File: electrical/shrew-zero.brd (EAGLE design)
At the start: 18 x 20 mm, 44 parts, among them IC1 LMR16006YQ3DDCTQ1, U1 ESP32-PICO-D4, U2 SX1280IMLTRT, X1 PIN-1X-BIG, X2 PIN-1X-BIG, Y1 2450FM07D0034001T, Y2 52MHz TCXO

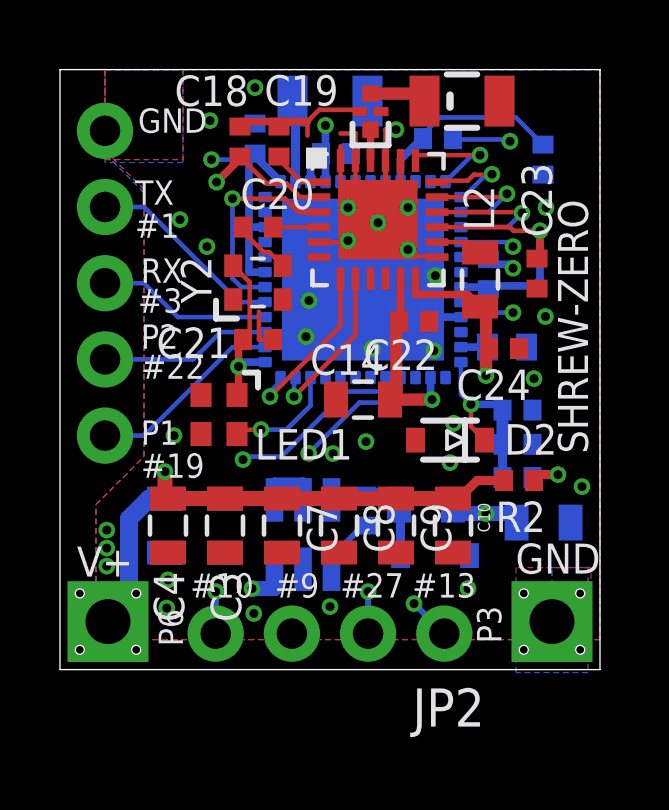
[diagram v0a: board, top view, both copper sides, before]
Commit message: shrew zero layout improvements
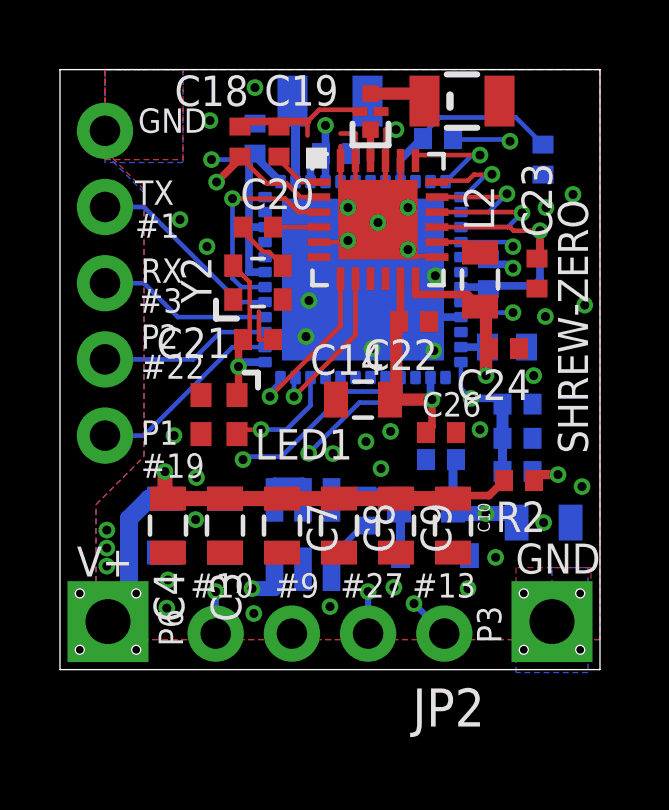
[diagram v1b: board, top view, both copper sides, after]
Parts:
- removed D2: 3V6, shrew-common:SOD-323
- added C25, C26: 470n, shrew-common:0402-REV
- moved R4 0.20 mm to (15.2, 7.71)
- moved C17 0.20 mm to (15.2, 8.85)
- moved R3 0.20 mm to (15.2, 6.60)
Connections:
- net 3.3V: now also C25.1, C26.1
- net BATT-ADC: no longer D2.1
- net GND: now also C25.2, C26.2; no longer D2.2
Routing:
- net GND: track 36.4 -> 33.7 mm, vias 31 -> 39
- net 3.3V: track 49.0 -> 51.6 mm
- net BATT-ADC: track 6.42 -> 4.84 mm

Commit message: shrew zero next prototype ready to mfg
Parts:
- added C27: 100n, shrew-common:0402-REV
- added C28: 0p5, shrew-common:0402-REV
- ANT1, ANT2: value 74889302450 -> ANT3216LL00R2400A
- moved C11 0.30 mm to (6.50, 17.4)
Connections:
- net 3.3V: now also C27.2
- net GND: now also C27.1, C28.1
- net N$1: now also C28.2
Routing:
- net GND: track 33.7 -> 38.9 mm, vias 39 -> 40
- net 3.3V: track 51.6 -> 53.6 mm, vias 8 -> 9
- net N$1: track 2.78 -> 4.04 mm

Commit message: shrew zero another mfg run
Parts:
- moved C11 0.30 mm to (6.50, 17.7)
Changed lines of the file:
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@@
 <grid distance="0.1" unitdist="mm" unit="mm" style="dots" multiple="10" display="yes" altdistance="0.01" altunitdist="mm" altunit="mm"/>
 <layers>
-<layer number="1" name="Top" color="4" fill="1" visible="yes" active="yes"/>
+<layer number="1" name="Top" color="4" fill="1" visible="no" active="yes"/>
 <layer number="2" name="Route2" color="1" fill="3" visible="no" active="yes"/>
 <layer number="3" name="Route3" color="4" fill="3" visible="no" active="no"/>
@@
 <layer number="13" name="Route13" color="4" fill="5" visible="no" active="no"/>
 <layer number="14" name="Route14" color="1" fill="6" visible="no" active="no"/>
-<layer number="15" name="Route15" color="4" fill="6" visible="yes" active="yes"/>
+<layer number="15" name="Route15" color="4" fill="6" visible="no" active="yes"/>
 <layer number="16" name="Bottom" color="1" fill="1" visible="yes" active="yes"/>
 <layer number="17" name="Pads" color="2" fill="1" visible="yes" active="yes"/>
@@
 <layer number="21" name="tPlace" color="7" fill="1" visible="yes" active="yes"/>
 <layer number="22" name="bPlace" color="7" fill="1" visible="yes" active="yes"/>
-<layer number="23" name="tOrigins" color="15" fill="1" visible="no" active="yes"/>
-<layer number="24" name="bOrigins" color="15" fill="1" visible="no" active="yes"/>
+<layer number="23" name="tOrigins" color="15" fill="1" visible="yes" active="yes"/>
+<layer number="24" name="bOrigins" color="15" fill="1" visible="yes" active="yes"/>
 <layer number="25" name="tNames" color="7" fill="1" visible="no" active="yes"/>
 <layer number="26" name="bNames" color="7" fill="1" visible="no" active="yes"/>
@@
 <attribute name="VALUE" x="14.1705" y="9.993" size="0.4064" layer="28" rot="MR180"/>
 </element>
-<element name="C11" library="shrew-common" package="0402-REV" value="100n" x="6.5" y="17.4" smashed="yes" rot="MR90">
-<attribute name="NAME" x="7.1985" y="16.511" size="0.4064" layer="26" rot="MR90"/>
-<attribute name="VALUE" x="5.357" y="16.3205" size="0.4064" layer="28" rot="MR90"/>
+<element name="C11" library="shrew-common" package="0402-REV" value="100n" x="6.5" y="17.7" smashed="yes" rot="MR90">
+<attribute name="NAME" x="7.1985" y="16.811" size="0.4064" layer="26" rot="MR90"/>
+<attribute name="VALUE" x="5.357" y="16.6205" size="0.4064" layer="28" rot="MR90"/>
 </element>
 <element name="C15" library="shrew-common" package="0402-REV" value="470n" x="16.1" y="17" smashed="yes" rot="MR90">
@@
 <wire x1="8.85" y1="17.5" x2="8.7" y2="17.2" width="0.254" layer="16"/>
 <wire x1="7.35" y1="16.265" x2="6.565" y2="17.05" width="0.254" layer="16"/>
-<wire x1="6.565" y1="17.05" x2="6.5" y2="16.9" width="0.254" layer="16"/>
+<wire x1="6.565" y1="17.05" x2="6.5" y2="17.2" width="0.254" layer="16"/>
 <wire x1="6.835" y1="14.75" x2="6.3" y2="14.75" width="0.254" layer="16"/>
 <wire x1="6.3" y1="14.75" x2="6.3" y2="17" width="0.254" layer="16"/>
 <wire x1="6.3" y1="17" x2="6.3" y2="17.05" width="0.254" layer="16"/>
-<wire x1="6.3" y1="17.05" x2="6.5" y2="16.9" width="0.254" layer="16"/>
+<wire x1="6.3" y1="17.05" x2="6.5" y2="17.2" width="0.254" layer="16"/>
 <via x="5.05" y="17" extent="1-16" drill="0.3" shape="octagon"/>
 <wire x1="5.05" y1="17" x2="6.3" y2="17" width="0.1524" layer="16"/>

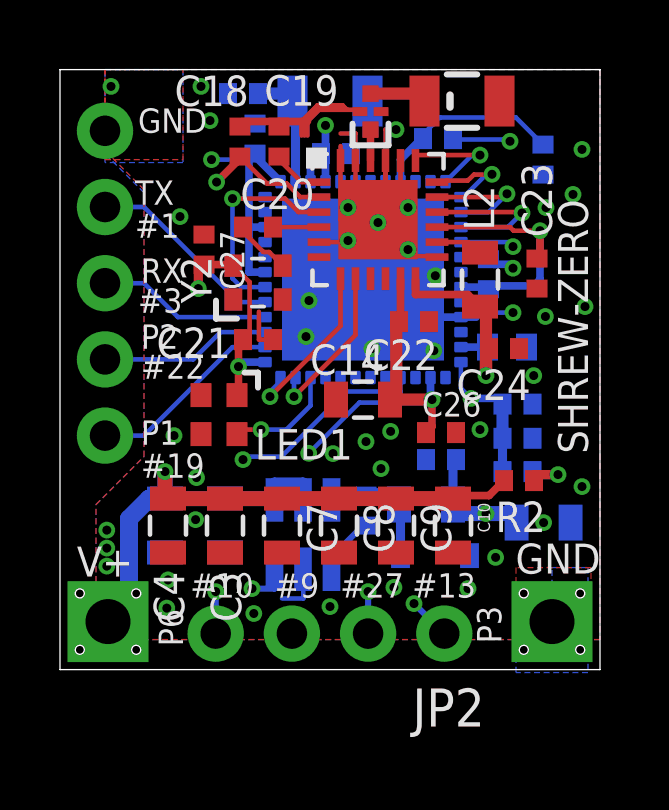
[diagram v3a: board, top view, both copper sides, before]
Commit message: PCB changes for better EMI emissions
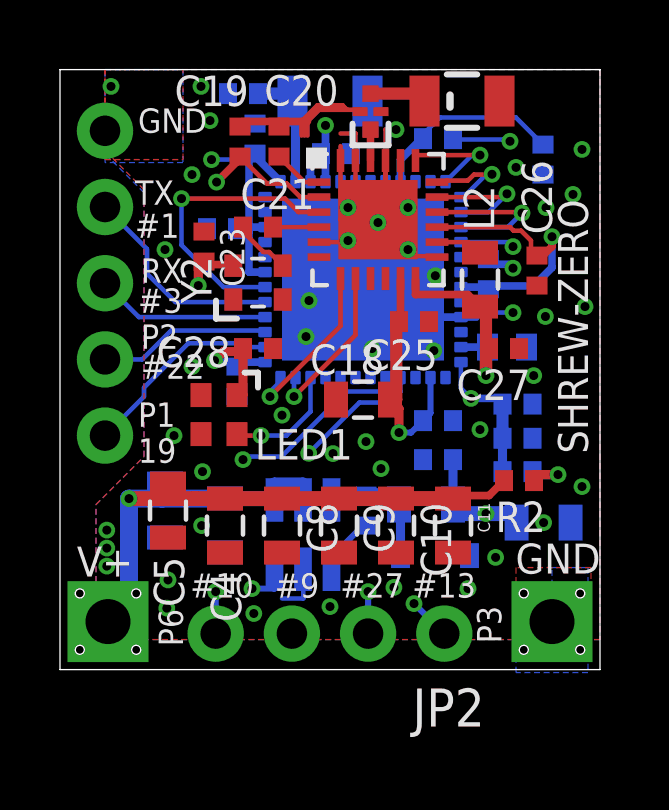
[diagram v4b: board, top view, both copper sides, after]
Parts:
- added C29: 470n, shrew-common:0402-REV
- added C30: DNP, shrew-common:0402-CAP
- C11: value 100n -> 10u; device shrew-common:0402-REV -> shrew-common:0805
- C14: value 10uF 25V -> 100n; device shrew-common:0805 -> shrew-common:0402-REV
- C15, C17, C25, C26: value 470n -> 100n
- C16: value DNP -> 100n; device shrew-common:0402-CAP -> shrew-common:0402-REV
- C18: value 10n -> 10uF 25V; device shrew-common:0402-REV -> shrew-common:0805
- C20: value 1n -> 10n
- C21: value 100n -> 1n
- C22, C27: value 100n -> 470n
- C24: value 470n -> 0p5
- C28: value 0p5 -> 100n
- C3: value 10u -> 470n; device shrew-common:0805 -> shrew-common:0402-REV
- U1: value ESP32-PICO-D4 -> SX1280IMLTRT; device shrew-core:PQFN50P700X700X104-49N -> shrew-core:QFN24_4X4_SEM
- U2: value SX1280IMLTRT -> ESP32-PICO-D4; device shrew-core:QFN24_4X4_SEM -> shrew-core:PQFN50P700X700X104-49N
- moved C11 14.5 mm to (13.1, 4.80), flipped to the top, turned to 270 degrees
- moved C24 12.2 mm to (6.10, 19.2), flipped to the bottom
- moved C23 11.1 mm to (4.80, 14.1), turned to 270 degrees
- moved C15 10.9 mm to (5.40, 14.7), turned to 0 degrees
- moved C27 10.5 mm to (14.8, 10.7), turned to 180 degrees
- moved C18 9.53 mm to (10.1, 9.00), turned to 180 degrees
- moved C16 9.07 mm to (5.90, 9.60), turned to 270 degrees
- moved C28 8.51 mm to (6.60, 10.7), flipped to the top
- moved C3 7.43 mm to (12.6, 7.00), flipped to the bottom, turned to 0 degrees
- moved C22 6.90 mm to (16.1, 17.0), flipped to the bottom, turned to 90 degrees
- moved C13 6.48 mm to (9.20, 17.2), turned to 180 degrees
- moved C26 6.28 mm to (15.9, 13.3), turned to 90 degrees
- moved C14 5.91 mm to (14.3, 13.2), flipped to the bottom, turned to 90 degrees
- moved C25 4.69 mm to (11.8, 11.6), flipped to the top, turned to 180 degrees
- moved C21 3.75 mm to (6.60, 14.8), turned to 0 degrees
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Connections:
- net +24V: now also C11.1; no longer C3.1
- net 3.3V: now also C15.1, C16.1, C17.1, C18.1, C25.2, C26.2, C28.2, C3.1, U1.11, U1.15, U2.1, U2.19, U2.26, U2.3, U2.37, U2.4, U2.43, U2.46; no longer C11.1, C21.2, C22.2, C25.1, C26.1, C27.2, U1.1, U1.19, U1.26, U1.3, U1.37, U1.4, U1.43, U1.46, U2.11, U2.15
- net AUX1: now also U2.38; no longer U1.38
- net AUX2: now also U2.39; no longer U1.39
- net BATT-ADC: now also C29.1, U2.24; no longer C17.1, U1.24
- net ESP-BOOT: now also C30.2, U2.23; no longer C16.2, U1.23
- net ESP-EN: now also C22.2, U2.9; no longer C15.2, U1.9
- net GND: now also C15.2, C16.2, C18.2, C20.1, C25.1, C26.1, C29.2, C30.1, U1.13, U1.20, U1.23, U1.24, U1.25, U1.5, U2.49; no longer C15.1, C16.1, C18.1, C21.1, C25.2, C26.2, U1.49, U2.13, U2.20, U2.23, U2.24, U2.25, U2.5
- net N$1: now also C24.2, U2.2; no longer C28.2, U1.2
- net N$11: now also C20.2, U1.1; no longer C19.2, U2.1
- net N$2: now also C21.1; no longer C20.1
- net N$3: now also C21.2, U1.4; no longer C20.2, U2.4
- net N$5: now also U2.17; no longer U1.17
- net N$6: now also U1.22; no longer U2.22
- net N$8: now also U2.22; no longer U1.22
- net N$9: now also U1.14; no longer U2.14
- net RADIO-BUSY: now also U1.7, U2.36; no longer U1.36, U2.7
- net RADIO-CS: now also U1.19, U2.12; no longer U1.12, U2.19
- net RADIO-DIO: now also U1.8, U2.35; no longer U1.35, U2.8
- net RADIO-RST: now also U1.3, U2.42; no longer U1.42, U2.3
- net RADIO-VDD: now also C19.2, C27.2, U1.12, U1.2; no longer C18.2, C24.2, U2.12, U2.2
- net RGBLED: now also U2.34; no longer U1.34
- net SIG1: now also U2.20; no longer U1.20
- net SIG2: now also U2.16; no longer U1.16
- net SIG3: now also U2.28; no longer U1.28
- net SIG4: now also U2.29; no longer U1.29
- net SPI-MISO: now also U1.16, U2.15; no longer U1.15, U2.16
- net SPI-MOSI: now also U1.17, U2.14; no longer U1.14, U2.17
- net SPI-SCK: now also U1.18, U2.13; no longer U1.13, U2.18
- net U0RXD: now also U2.40; no longer U1.40
- net U0TXD: now also U2.41; no longer U1.41
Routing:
- net GND: track 38.9 -> 59.8 mm, vias 40 -> 43
- net RADIO-RST: track 6.93 -> 9.68 mm
- net +24V: track 24.3 -> 25.1 mm
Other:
- board text added: "19"

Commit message: shrew zero added reverse protection diode
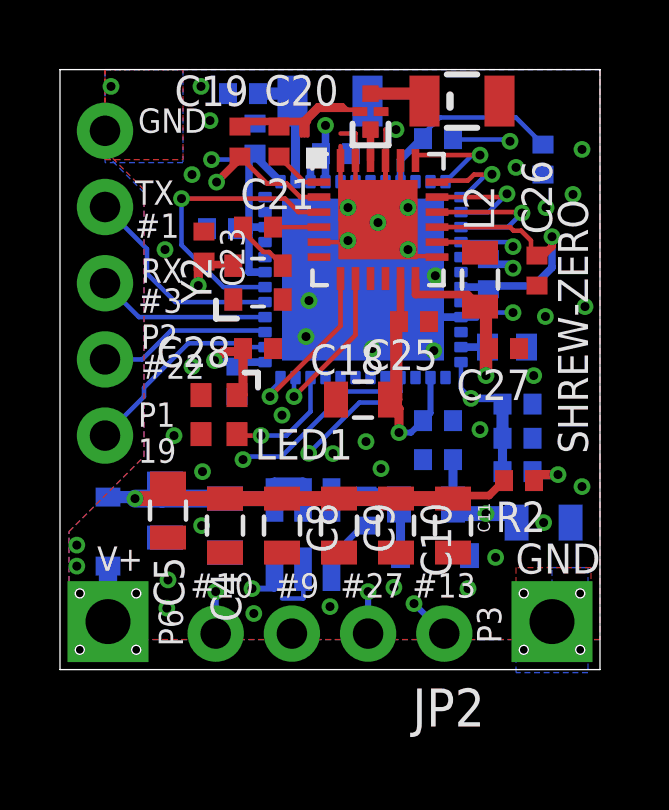
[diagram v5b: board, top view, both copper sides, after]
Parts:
- added D2: C406049, shrew-common:SOD-323
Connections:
- new net N$12: D2.2, X1.1
- net +24V: now also D2.1; no longer X1.1
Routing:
- net +24V: track 25.1 -> 21.3 mm
- net N$12: track 0.00 -> 1.85 mm
- net GND: vias 43 -> 42
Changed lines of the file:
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@@
 <layer number="19" name="Unrouted" color="6" fill="1" visible="yes" active="yes"/>
 <layer number="20" name="Dimension" color="15" fill="1" visible="yes" active="yes"/>
-<layer number="21" name="tPlace" color="7" fill="1" visible="no" active="yes"/>
-<layer number="22" name="bPlace" color="7" fill="1" visible="no" active="yes"/>
-<layer number="23" name="tOrigins" color="15" fill="1" visible="no" active="yes"/>
-<layer number="24" name="bOrigins" color="15" fill="1" visible="no" active="yes"/>
+<layer number="21" name="tPlace" color="7" fill="1" visible="yes" active="yes"/>
+<layer number="22" name="bPlace" color="7" fill="1" visible="yes" active="yes"/>
+<layer number="23" name="tOrigins" color="15" fill="1" visible="yes" active="yes"/>
+<layer number="24" name="bOrigins" color="15" fill="1" visible="yes" active="yes"/>
 <layer number="25" name="tNames" color="7" fill="1" visible="no" active="yes"/>
 <layer number="26" name="bNames" color="7" fill="1" visible="no" active="yes"/>
@@
 <wire x1="0" y1="20" x2="0" y2="0" width="0" layer="20"/>
 <text x="16.6" y="3.7" size="1" layer="21" font="vector" align="center">GND</text>
-<text x="1.5" y="3.6" size="1" layer="21" font="vector" align="center">V+</text>
-<text x="1.2" y="3.6" size="1" layer="22" font="vector" rot="MR0" align="center">V+</text>
+<text x="2" y="3.7" size="0.8128" layer="21" font="vector" align="center">V+</text>
+<text x="2.8" y="3.4" size="0.8128" layer="22" font="vector" rot="MR0" align="center">V+</text>
 <text x="2.4" y="18.3" size="0.8128" layer="22" rot="MR180" align="center-left">GND</text>
 <text x="2.5" y="15.9" size="0.8128" layer="22" rot="MR180" align="center-left">TX</text>
@@
 <element name="C15" library="shrew-common" package="0402-REV" value="100n" x="5.4" y="14.7" rot="MR0"/>
 <element name="C16" library="shrew-common" package="0402-REV" value="100n" x="5.9" y="9.6" rot="MR270"/>
+<element name="D2" library="shrew-common" package="SOD-323" value="C406049" x="1.6" y="4.6" rot="MR270"/>
 </elements>
 <signals>
@@
 <contactref element="C14" pad="2"/>
 <polygon width="0.1524" layer="1" spacing="0.1524" isolate="0.1524" rank="5">
-<vertex x="1.2" y="1"/>
-<vertex x="1.2" y="5.5"/>
+<vertex x="0.3" y="1"/>
+<vertex x="0.3" y="4.6"/>
 <vertex x="2.8" y="7.1"/>
 <vertex x="2.8" y="16"/>
@@
 </polygon>
 <polygon width="0.1524" layer="16" spacing="0.1524" isolate="0.1524" rank="5">
-<vertex x="1.2" y="1"/>
-<vertex x="1.2" y="5.5"/>
+<vertex x="0.3" y="1"/>
+<vertex x="0.3" y="4.6"/>
 <vertex x="2.8" y="7.1"/>
 <vertex x="2.8" y="15.9"/>
@@
 <via x="13.6" y="2.7" extent="1-16" drill="0.3" shape="octagon"/>
 <via x="3.56" y="2.05" extent="1-16" drill="0.3" shape="octagon"/>
-<via x="1.56" y="3.45" extent="1-16" drill="0.3" shape="octagon"/>
-<via x="1.56" y="4.05" extent="1-16" drill="0.3" shape="octagon"/>
-<via x="1.56" y="4.65" extent="1-16" drill="0.3" shape="octagon"/>
+<via x="0.56" y="4.15" extent="1-16" drill="0.3" shape="octagon"/>
+<via x="0.56" y="3.45" extent="1-16" drill="0.3" shape="octagon"/>
 <polygon width="0.254" layer="15" spacing="0.254" isolate="0.254">
 <vertex x="0" y="1"/>
@@
 </signal>
 <signal name="+24V">
-<contactref element="X1" pad="1"/>
 <contactref element="C4" pad="1"/>
 <contactref element="C6" pad="1"/>
@@
 <wire x1="7.15" y1="5.655" x2="7.15" y2="5.7" width="0.4064" layer="16"/>
 <wire x1="7.15" y1="5.7" x2="5.5" y2="5.7" width="0.5" layer="16"/>
-<wire x1="1.6" y1="1.6" x2="2.3" y2="2.3" width="0.6" layer="16"/>
-<wire x1="2.3" y1="2.3" x2="2.3" y2="5.7" width="0.6" layer="16"/>
-<via x="2.3" y="5.7" extent="1-16" drill="0.3" shape="octagon"/>
+<via x="2.5" y="5.7" extent="1-16" drill="0.3" shape="octagon"/>
 <wire x1="13.1" y1="5.7" x2="13.5" y2="5.7" width="0.254" layer="1"/>
 <wire x1="13.5" y1="5.7" x2="13.5" y2="5.8" width="0.254" layer="1"/>
 <wire x1="13.5" y1="5.8" x2="14.3" y2="5.8" width="0.254" layer="1"/>
 <wire x1="14.3" y1="5.8" x2="14.8" y2="6.3" width="0.254" layer="1"/>
-<wire x1="2.3" y1="5.7" x2="3.4" y2="5.7" width="0.6" layer="16"/>
+<wire x1="2.5" y1="5.7" x2="3.4" y2="5.7" width="0.6" layer="16"/>
 <wire x1="3.4" y1="5.7" x2="5.5" y2="5.7" width="0.6" layer="16"/>
 <wire x1="3.5" y1="6.2" x2="3.4" y2="6.1" width="0.5" layer="16"/>
 <wire x1="3.4" y1="6.1" x2="3.4" y2="5.7" width="0.5" layer="16"/>
-<wire x1="5.5" y1="5.7" x2="4.5" y2="5.7" width="0.5" layer="1"/>
-<wire x1="3.6" y1="5.7" x2="2.3" y2="5.7" width="0.5" layer="1"/>
+<wire x1="5.5" y1="5.7" x2="3.6" y2="5.7" width="0.5" layer="1"/>
+<wire x1="3.6" y1="5.7" x2="2.5" y2="5.7" width="0.5" layer="1"/>
 <wire x1="3.6" y1="6.2" x2="3.6" y2="5.7" width="0.5" layer="1"/>
-<wire x1="3.6" y1="5.7" x2="4.5" y2="5.7" width="0.5" layer="1"/>
+<contactref element="D2" pad="1"/>
+<wire x1="1.6" y1="5.75" x2="2.5" y2="5.75" width="0.4064" layer="16"/>
+<wire x1="2.5" y1="5.75" x2="2.5" y2="5.7" width="0.4064" layer="16"/>
 </signal>
 <signal name="N$4">
@@
 <wire x1="11.3" y1="5.8" x2="11.3" y2="5.5" width="0.5" layer="16"/>
 </signal>
+<signal name="N$12">
+<contactref element="X1" pad="1"/>
+<contactref element="D2" pad="2"/>
+<wire x1="1.6" y1="1.6" x2="1.6" y2="3.45" width="0.6096" layer="16"/>
+</signal>
 </signals>
